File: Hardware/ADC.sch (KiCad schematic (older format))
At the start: 7 parts, among them U2 NCP51460SN33T1G, U3 MCP3002

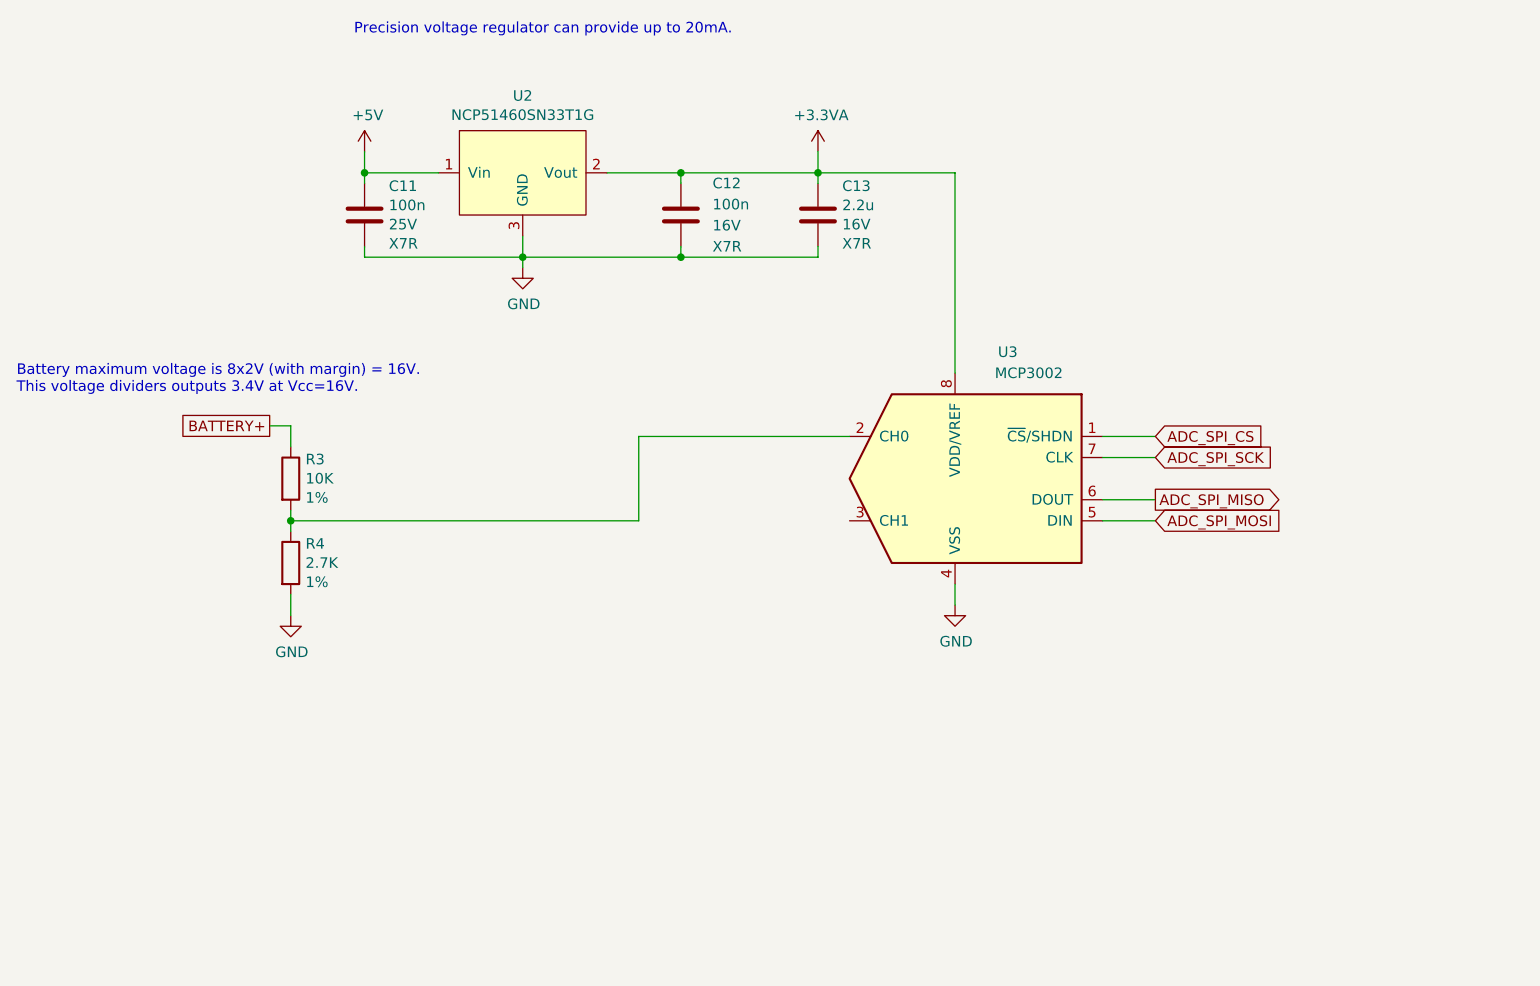
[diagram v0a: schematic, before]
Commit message: [Hardware] Added LDR to schematic.
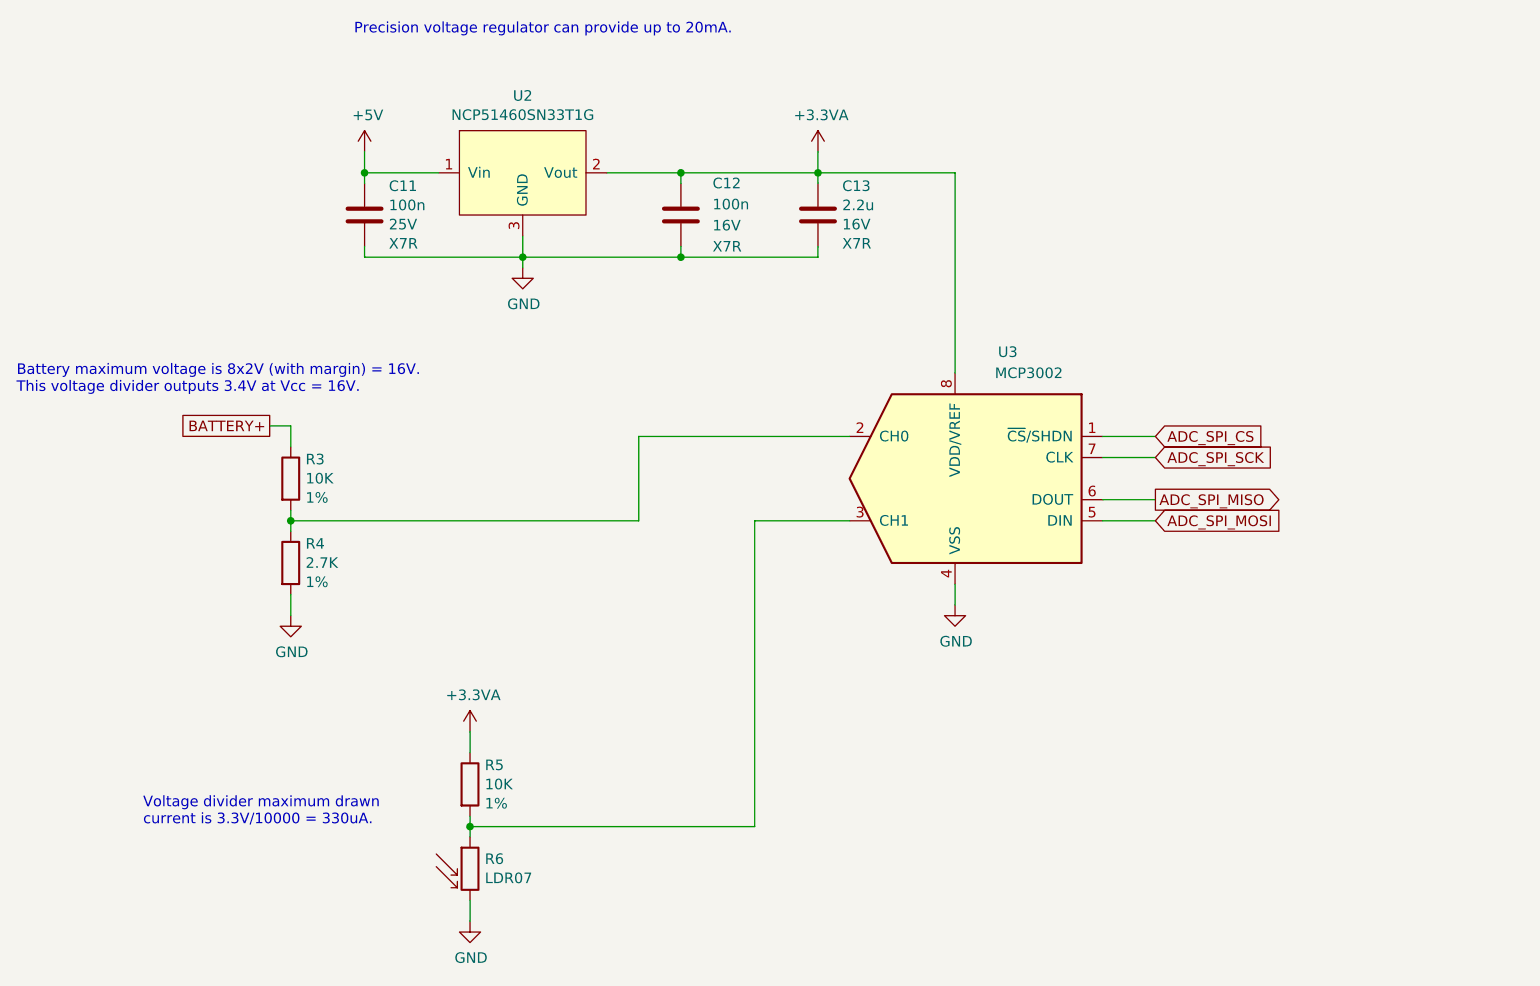
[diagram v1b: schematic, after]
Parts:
- added R5: 10K, Resistor_SMD:R_1210_3225Metric_Pad1.42x2.65mm_HandSolder, symbol Device:R
- added R6: LDR07, OptoDevice:R_LDR_5.1x4.3mm_P3.4mm_Vertical, symbol Sensor_Optical:LDR07
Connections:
- net +3.3VA: now also R5.1
- net GND: now also R6.2
- net at U3.3 (CH1): now also R5.2, R6.1
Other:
- note added: "Battery maximum voltage is 8x2V (with margin) = 16V.\nThis voltage divider outputs 3.4V at Vcc = 16V."
- note added: "Voltage divider maximum drawn\ncurrent is 3.3V/10000 = 330uA."
- note removed: "Battery maximum voltage is 8x2V (with margin) = 16V.\nThis voltage dividers outputs 3.4V at Vcc=16V."
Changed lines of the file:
@@
 BATTERY+
 Text Notes 1550 3200 0    50   ~ 0
-Battery maximum voltage is 8x2V (with margin) = 16V.\nThis voltage dividers outputs 3.4V at Vcc=16V.
+Battery maximum voltage is 8x2V (with margin) = 16V.\nThis voltage divider outputs 3.4V at Vcc = 16V.
 $Comp
 L Device:R R3
@@
 Wire Wire Line
 	2850 3800 2850 3850
+$Comp
+L Device:R R5
+U 1 1 5F258418
+P 3700 5050
+F 0 "R5" H 3770 5141 50  0000 L CNN
+F 1 "10K" H 3770 5050 50  0000 L CNN
+F 2 "Resistor_SMD:R_1210_3225Metric_Pad1.42x2.65mm_HandSolder" V 3630 5050 50  0001 C CNN
+F 3 "~" H 3700 5050 50  0001 C CNN
+F 4 "1%" H 3770 4959 50  0000 L CNN "Value2"
+	1    3700 5050
+	1    0    0    -1
+$EndComp
+$Comp
+L power:+3.3VA #PWR012
+U 1 1 5F259335
+P 3700 4800
+F 0 "#PWR012" H 3700 4650 50  0001 C CNN
+F 1 "+3.3VA" H 3715 4973 50  0000 C CNN
+F 2 "" H 3700 4800 50  0001 C CNN
+F 3 "" H 3700 4800 50  0001 C CNN
+	1    3700 4800
+	1    0    0    -1
+$EndComp
+Text Notes 2150 5250 0    50   ~ 0
+Voltage divider maximum drawn\ncurrent is 3.3V/10000 = 330uA.
+$Comp
+L Sensor_Optical:LDR07 R6
+U 1 1 5F25AAB7
+P 3700 5450
+F 0 "R6" H 3770 5496 50  0000 L CNN
+F 1 "LDR07" H 3770 5405 50  0000 L CNN
+F 2 "OptoDevice:R_LDR_5.1x4.3mm_P3.4mm_Vertical" V 3875 5450 50  0001 C CNN
+F 3 "http://www.tme.eu/de/Document/f2e3ad76a925811312d226c31da4cd7e/LDR07.pdf" H 3700 5400 50  0001 C CNN
+	1    3700 5450
+	1    0    0    -1
+$EndComp
+$Comp
+L power:GND #PWR?
+U 1 1 5F20193C
+P 3700 5700
+F 0 "#PWR?" H 3700 5450 50  0001 C CNN
+F 1 "GND" H 3705 5527 50  0000 C CNN
+F 2 "" H 3700 5700 50  0001 C CNN
+F 3 "" H 3700 5700 50  0001 C CNN
+	1    3700 5700
+	1    0    0    -1
+$EndComp
+Wire Wire Line
+	3700 5700 3700 5600
+Wire Wire Line
+	3700 5300 3700 5250
+Wire Wire Line
+	3700 4900 3700 4800
+Wire Wire Line
+	3700 5250 5050 5250
+Wire Wire Line
+	5050 5250 5050 3800
+Wire Wire Line
+	5050 3800 5500 3800
+Connection ~ 3700 5250
+Wire Wire Line
+	3700 5250 3700 5200
 $EndSCHEMATC

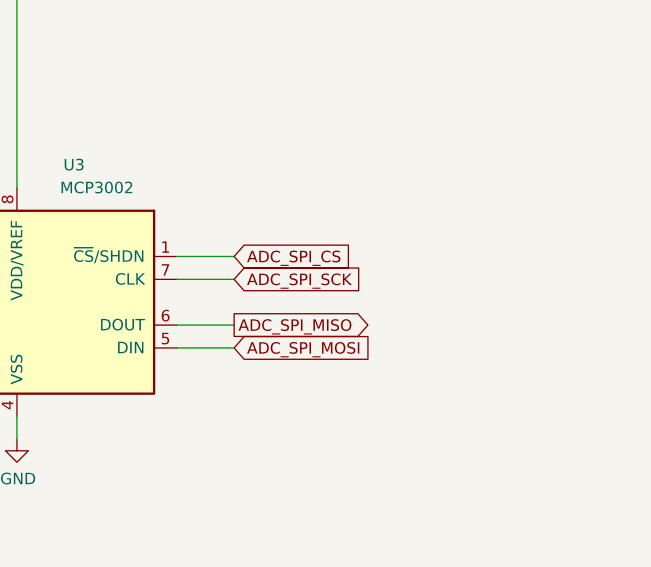
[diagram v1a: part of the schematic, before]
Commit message: [Hardware] Connected ADC to Raspberry Pi through SPI bus.
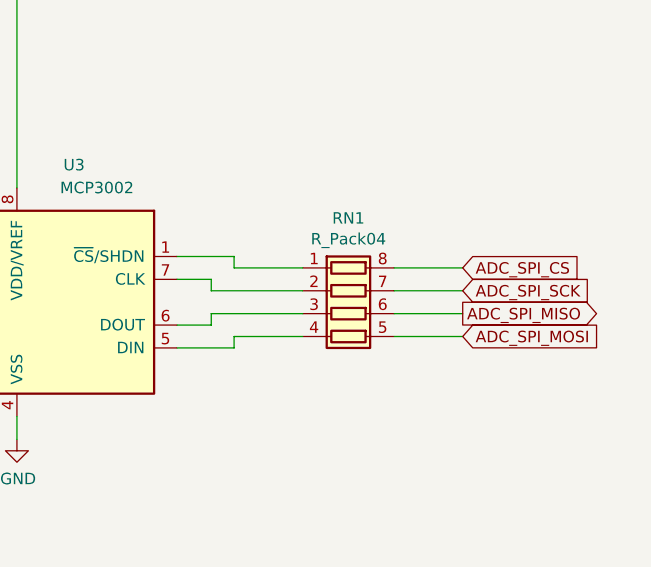
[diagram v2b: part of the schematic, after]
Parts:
- added RN1: R_Pack04, Resistor_SMD:R_Array_Convex_4x1206, symbol Device:R_Pack04
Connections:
- net ADC_SPI_CS: now also RN1.8 (R1.2); no longer U3.1 (~CS~/SHDN)
- net ADC_SPI_MISO: now also RN1.6 (R3.2); no longer U3.6 (DOUT)
- net ADC_SPI_MOSI: now also RN1.5 (R4.2); no longer U3.5 (DIN)
- net ADC_SPI_SCK: now also RN1.7 (R2.2); no longer U3.7 (CLK)
- new net: RN1.1 (R1.1), U3.1 (~CS~/SHDN)
- new net: RN1.2 (R2.1), U3.7 (CLK)
- new net: RN1.3 (R3.1), U3.6 (DOUT)
- new net: RN1.4 (R4.1), U3.5 (DIN)
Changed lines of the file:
@@
 Wire Wire Line
 	6000 4200 6000 4100
-Text GLabel 6950 3400 2    50   Input ~ 0
+Text GLabel 7950 3450 2    50   Input ~ 0
 ADC_SPI_CS
-Wire Wire Line
-	6950 3400 6700 3400
-Text GLabel 6950 3500 2    50   Input ~ 0
+Text GLabel 7950 3550 2    50   Input ~ 0
 ADC_SPI_SCK
-Wire Wire Line
-	6950 3500 6700 3500
-Text GLabel 6950 3700 2    50   Output ~ 0
+Text GLabel 7950 3650 2    50   Output ~ 0
 ADC_SPI_MISO
-Wire Wire Line
-	6950 3700 6700 3700
-Text GLabel 6950 3800 2    50   Input ~ 0
+Text GLabel 7950 3750 2    50   Input ~ 0
 ADC_SPI_MOSI
-Wire Wire Line
-	6950 3800 6700 3800
 $Comp
 L power:+3.3VA #PWR09
@@
 $EndComp
 $Comp
-L power:GND #PWR?
+L power:GND #PWR013
 U 1 1 5F20193C
 P 3700 5700
-F 0 "#PWR?" H 3700 5450 50  0001 C CNN
+F 0 "#PWR013" H 3700 5450 50  0001 C CNN
 F 1 "GND" H 3705 5527 50  0000 C CNN
 F 2 "" H 3700 5700 50  0001 C CNN
@@
 Wire Wire Line
 	3700 5250 3700 5200
+$Comp
+L Device:R_Pack04 RN1
+U 1 1 5F207575
+P 7450 3650
+F 0 "RN1" V 7033 3650 50  0000 C CNN
+F 1 "R_Pack04" V 7124 3650 50  0000 C CNN
+F 2 "Resistor_SMD:R_Array_Convex_4x1206" V 7725 3650 50  0001 C CNN
+F 3 "~" H 7450 3650 50  0001 C CNN
+F 4 "MP000987" V 7450 3650 50  0001 C CNN "Value2"
+F 5 "Multicomp" V 7450 3650 50  0001 C CNN "Manufacturer"
+	1    7450 3650
+	0    1    1    0
+$EndComp
+Wire Wire Line
+	6700 3700 6850 3700
+Wire Wire Line
+	6850 3700 6850 3650
+Wire Wire Line
+	6850 3650 7250 3650
+Wire Wire Line
+	6950 3800 6950 3750
+Wire Wire Line
+	6950 3750 7250 3750
+Wire Wire Line
+	6700 3800 6950 3800
+Wire Wire Line
+	6700 3500 6850 3500
+Wire Wire Line
+	6850 3500 6850 3550
+Wire Wire Line
+	6850 3550 7250 3550
+Wire Wire Line
+	6700 3400 6950 3400
+Wire Wire Line
+	6950 3400 6950 3450
+Wire Wire Line
+	6950 3450 7250 3450
+Wire Wire Line
+	7650 3750 7950 3750
+Wire Wire Line
+	7650 3650 7950 3650
+Wire Wire Line
+	7650 3550 7950 3550
+Wire Wire Line
+	7650 3450 7950 3450
 $EndSCHEMATC

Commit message: [Hardware] Added servomotors supply parts and connected them to Raspberry Pi PWMs.
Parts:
- U3: footprint (none) -> Package_SO:SOIC-8_3.9x4.9mm_P1.27mm
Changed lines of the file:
@@
 F 0 "U3" H 6250 4200 50  0000 C CNN
 F 1 "MCP3002" H 6350 4100 50  0000 C CNN
-F 2 "" H 6000 3500 50  0001 C CNN
+F 2 "Package_SO:SOIC-8_3.9x4.9mm_P1.27mm" H 6000 3500 50  0001 C CNN
 F 3 "http://ww1.microchip.com/downloads/en/DeviceDoc/21294E.pdf" H 6000 3800 50  0001 C CNN
 	1    6000 3600

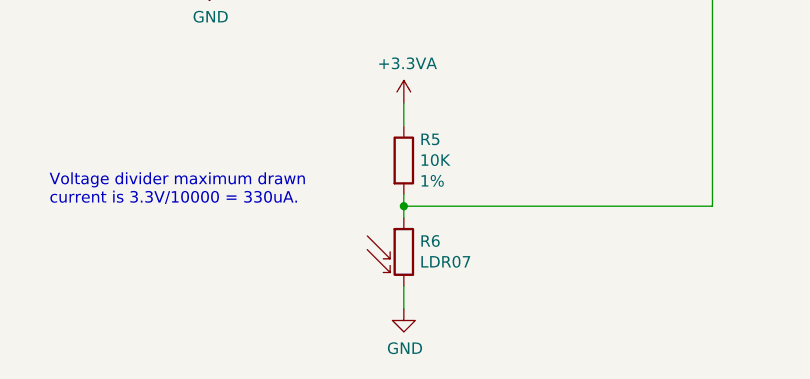
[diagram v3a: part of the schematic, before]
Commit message: [Hardware] Added camera board.
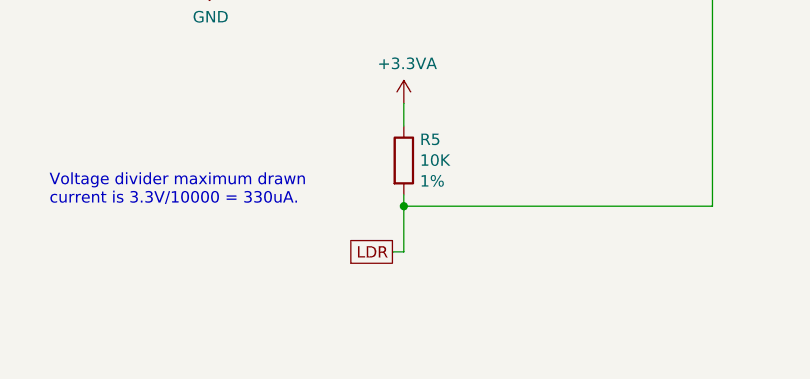
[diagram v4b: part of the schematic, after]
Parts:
- removed R6: LDR07, OptoDevice:R_LDR_5.1x4.3mm_P3.4mm_Vertical, symbol Sensor_Optical:LDR07
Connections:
- net LDR: now reaches R5.2, U3.3 (CH1)
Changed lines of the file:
@@
 $Descr A4 11693 8268
 encoding utf-8
-Sheet 4 4
+Sheet 4 5
 Title "Analog-to-digital converter"
 Date "2020-07-27"
@@
 Text Notes 2150 5250 0    50   ~ 0
 Voltage divider maximum drawn\ncurrent is 3.3V/10000 = 330uA.
-$Comp
-L Sensor_Optical:LDR07 R6
-U 1 1 5F25AAB7
-P 3700 5450
-F 0 "R6" H 3770 5496 50  0000 L CNN
-F 1 "LDR07" H 3770 5405 50  0000 L CNN
-F 2 "OptoDevice:R_LDR_5.1x4.3mm_P3.4mm_Vertical" V 3875 5450 50  0001 C CNN
-F 3 "http://www.tme.eu/de/Document/f2e3ad76a925811312d226c31da4cd7e/LDR07.pdf" H 3700 5400 50  0001 C CNN
-	1    3700 5450
-	1    0    0    -1
-$EndComp
-$Comp
-L power:GND #PWR013
-U 1 1 5F20193C
-P 3700 5700
-F 0 "#PWR013" H 3700 5450 50  0001 C CNN
-F 1 "GND" H 3705 5527 50  0000 C CNN
-F 2 "" H 3700 5700 50  0001 C CNN
-F 3 "" H 3700 5700 50  0001 C CNN
-	1    3700 5700
-	1    0    0    -1
-$EndComp
-Wire Wire Line
-	3700 5700 3700 5600
-Wire Wire Line
-	3700 5300 3700 5250
 Wire Wire Line
 	3700 4900 3700 4800
@@
 Wire Wire Line
 	7650 3450 7950 3450
+Text GLabel 3650 5450 0    50   UnSpc ~ 0
+LDR
+Wire Wire Line
+	3700 5450 3650 5450
+Wire Wire Line
+	3700 5250 3700 5450
 $EndSCHEMATC

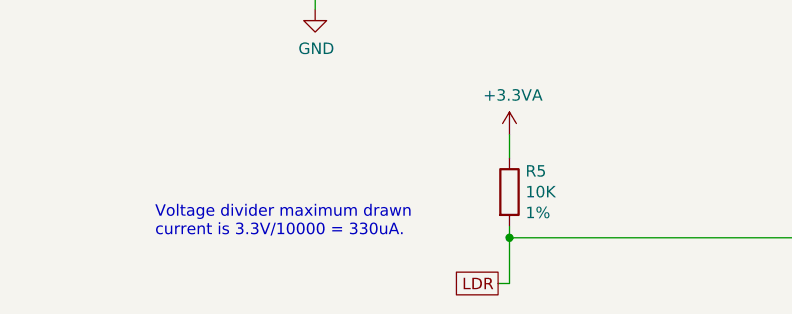
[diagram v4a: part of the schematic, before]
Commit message: [Hardware] Added a transistor to enable leds control from Raspberry Pi.
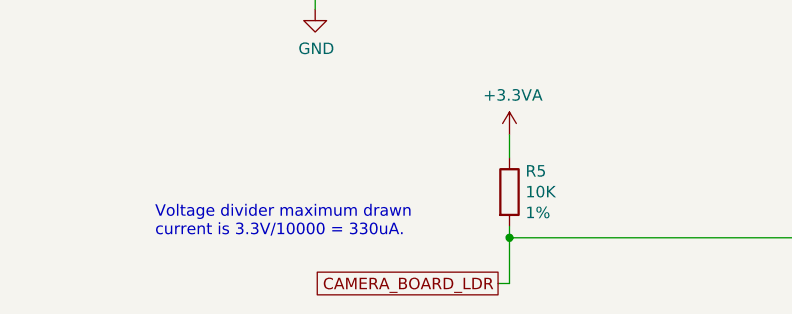
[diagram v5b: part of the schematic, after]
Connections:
- net LDR renamed CAMERA_BOARD_LDR
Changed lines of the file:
@@
 	7650 3450 7950 3450
 Text GLabel 3650 5450 0    50   UnSpc ~ 0
-LDR
+CAMERA_BOARD_LDR
 Wire Wire Line
 	3700 5450 3650 5450

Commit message: [Hardware] Renamed 'camera board' to 'front board' as this board is not only carrying the camera.
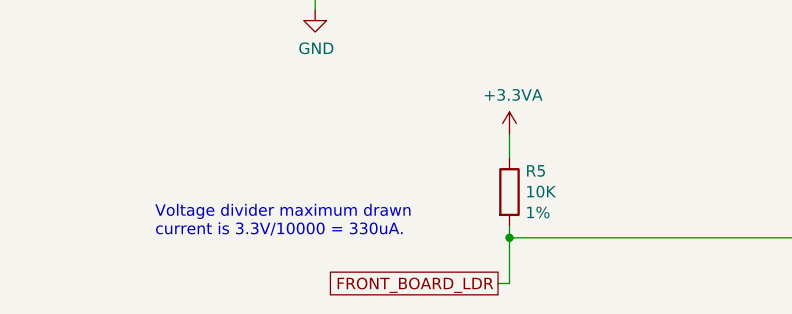
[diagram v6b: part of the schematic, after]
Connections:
- net CAMERA_BOARD_LDR renamed FRONT_BOARD_LDR
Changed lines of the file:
@@
 	7650 3450 7950 3450
 Text GLabel 3650 5450 0    50   UnSpc ~ 0
-CAMERA_BOARD_LDR
+FRONT_BOARD_LDR
 Wire Wire Line
 	3700 5450 3650 5450

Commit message: [Hardware] Fixed ADC voltage reference decoupling capacitors footprints.
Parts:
- C68, C69: footprint Capacitor_SMD:C_0603_1608Metric -> Capacitor_SMD:C_1206_3216Metric
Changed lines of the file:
@@
 F 0 "C11" H 3315 2487 50  0000 L CNN
 F 1 "100n" H 3315 2396 50  0000 L CNN
-F 2 "Capacitor_SMD:C_0603_1608Metric" H 3238 2200 50  0001 C CNN
+F 2 "Capacitor_SMD:C_1206_3216Metric" H 3238 2200 50  0001 C CNN
 F 3 "~" H 3200 2350 50  0001 C CNN
 F 4 "25V" H 3315 2305 50  0000 L CNN "Value2"
@@
 F 0 "C12" H 4850 2500 50  0000 L CNN
 F 1 "100n" H 4850 2400 50  0000 L CNN
-F 2 "Capacitor_SMD:C_0603_1608Metric" H 4738 2200 50  0001 C CNN
+F 2 "Capacitor_SMD:C_1206_3216Metric" H 4738 2200 50  0001 C CNN
 F 3 "~" H 4700 2350 50  0001 C CNN
 F 4 "16V" H 4850 2300 50  0000 L CNN "Value2"

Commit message: [Hardware] Fixed bad footprints and duplicated break tab footprints.
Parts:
- C68, C69, C7: footprint Capacitor_SMD:C_1206_3216Metric -> Capacitor_SMD:C_1206_3216Metric_Pad1.42x1.75mm_HandSolder
- R3, R4, R5: footprint Resistor_SMD:R_1210_3225Metric_Pad1.42x2.65mm_HandSolder -> Resistor_SMD:R_1206_3216Metric_Pad1.42x1.75mm_HandSolder
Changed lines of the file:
@@
 F 0 "C13" H 5465 2487 50  0000 L CNN
 F 1 "2.2u" H 5465 2396 50  0000 L CNN
-F 2 "Capacitor_SMD:C_1206_3216Metric" H 5388 2200 50  0001 C CNN
+F 2 "Capacitor_SMD:C_1206_3216Metric_Pad1.42x1.75mm_HandSolder" H 5388 2200 50  0001 C CNN
 F 3 "~" H 5350 2350 50  0001 C CNN
 F 4 "16V" H 5465 2305 50  0000 L CNN "Value2"
@@
 F 0 "C11" H 3315 2487 50  0000 L CNN
 F 1 "100n" H 3315 2396 50  0000 L CNN
-F 2 "Capacitor_SMD:C_1206_3216Metric" H 3238 2200 50  0001 C CNN
+F 2 "Capacitor_SMD:C_1206_3216Metric_Pad1.42x1.75mm_HandSolder" H 3238 2200 50  0001 C CNN
 F 3 "~" H 3200 2350 50  0001 C CNN
 F 4 "25V" H 3315 2305 50  0000 L CNN "Value2"
@@
 F 0 "C12" H 4850 2500 50  0000 L CNN
 F 1 "100n" H 4850 2400 50  0000 L CNN
-F 2 "Capacitor_SMD:C_1206_3216Metric" H 4738 2200 50  0001 C CNN
+F 2 "Capacitor_SMD:C_1206_3216Metric_Pad1.42x1.75mm_HandSolder" H 4738 2200 50  0001 C CNN
 F 3 "~" H 4700 2350 50  0001 C CNN
 F 4 "16V" H 4850 2300 50  0000 L CNN "Value2"
@@
 F 0 "R3" H 2920 3691 50  0000 L CNN
 F 1 "10K" H 2920 3600 50  0000 L CNN
-F 2 "Resistor_SMD:R_1210_3225Metric_Pad1.42x2.65mm_HandSolder" V 2780 3600 50  0001 C CNN
+F 2 "Resistor_SMD:R_1206_3216Metric_Pad1.42x1.75mm_HandSolder" V 2780 3600 50  0001 C CNN
 F 3 "~" H 2850 3600 50  0001 C CNN
 F 4 "1%" H 2920 3509 50  0000 L CNN "Value2"
@@
 F 0 "R4" H 2920 4091 50  0000 L CNN
 F 1 "2.7K" H 2920 4000 50  0000 L CNN
-F 2 "Resistor_SMD:R_1210_3225Metric_Pad1.42x2.65mm_HandSolder" V 2780 4000 50  0001 C CNN
+F 2 "Resistor_SMD:R_1206_3216Metric_Pad1.42x1.75mm_HandSolder" V 2780 4000 50  0001 C CNN
 F 3 "~" H 2850 4000 50  0001 C CNN
 F 4 "1%" H 2920 3909 50  0000 L CNN "Value2"
@@
 F 0 "R5" H 3770 5141 50  0000 L CNN
 F 1 "10K" H 3770 5050 50  0000 L CNN
-F 2 "Resistor_SMD:R_1210_3225Metric_Pad1.42x2.65mm_HandSolder" V 3630 5050 50  0001 C CNN
+F 2 "Resistor_SMD:R_1206_3216Metric_Pad1.42x1.75mm_HandSolder" V 3630 5050 50  0001 C CNN
 F 3 "~" H 3700 5050 50  0001 C CNN
 F 4 "1%" H 3770 4959 50  0000 L CNN "Value2"
